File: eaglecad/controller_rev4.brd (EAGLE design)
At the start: 70 x 29.5 mm, 85 parts, among them J1 1.27MM-SWD-CONNECTOR, U101 TCAN330, U200 TPS63070, U300 STSPIN230, U301 TSV991ILT, U302 AS5047P, U400 STSPIN250, U401 TSV991ILT, X101 ABM10-16MHz

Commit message: Prelim final rev completed + design overhaul
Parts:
- removed J1: 1.27MM-SWD-CONNECTOR, J-CNC-3220-10-0100-00-ARM-SWD-port:1.27MM_2X5
- removed JP1, JP2: (no value), pinhead:1X02
- removed JP103: (no value), SparkFun-Connectors:6_PIN_SERIAL_TARGET_SIDE_W_SILK
- removed R310, R311, R415, R416: 0.68, oresat-rcl:.0805-B-NOSILK
- removed R312, R313, R417, R418: 2.2k, rcl_custom:.0402-B-NOSILK
- removed R315: 10k, rcl_custom:.0402-B-NOSILK
- added JP101, JP501: (no value), pinhead:1X02
- added JP502: (no value), SparkFun-Connectors:6_PIN_SERIAL_TARGET_SIDE_W_SILK
- added JP503: 1.27MM-SWD-CONNECTOR, J-CNC-3220-10-0100-00-ARM-SWD-port:1.27MM_2X5
- added R303, R307: 2.2k, rcl_custom:.0402-B-NOSILK
- added R304: 680, rcl_custom:.0402-B-NOSILK
- added R305, R306, R411, R412: 0.68, oresat-rcl:.0805-B-NOSILK
- added R403, R404: 330, rcl_custom:.0402-B-NOSILK
- C306: value 680p -> 4.7u; device rcl_custom:.0402-B-NOSILK -> oresat-rcl:.0603-B-NOSILK
- C307, C408: value 680p -> 100n
- C308: value 100n -> 680p
- C309, C410: value 4.7u -> 680p; device oresat-rcl:.0603-B-NOSILK -> rcl_custom:.0402-B-NOSILK
- C406: value 22n -> 2.2n
- C407: value 2.2n -> 22n
- C409: value 100n -> 4.7u; device rcl_custom:.0402-B-NOSILK -> oresat-rcl:.0603-B-NOSILK
- R309: value 680 -> 10k
- R405: value 330 -> 100k
- R406: value 330 -> 18k
- R409: value 100k -> 2.2k
- R410: value 18k -> 680
- R414: value 680 -> 2.2k
- moved R309 44.4 mm to (20.0, 22.5), flipped to the bottom
- moved C306 43.8 mm to (24.0, 23.7), turned to 180 degrees
- moved C307 41.4 mm to (26.1, 24.6)
- moved R406 40.0 mm to (27.4, 9.01), turned to 270 degrees
- moved R405 40.0 mm to (26.4, 9.01)
- moved U301 39.5 mm to (23.8, 26.0)
- moved TP1 38.3 mm to (12.8, 6.45)
- moved C301 38.0 mm to (12.1, 20.3), flipped to the bottom, turned to 180 degrees
- moved R308 37.1 mm to (25.1, 28.1), turned to 0 degrees
- moved C309 37.0 mm to (26.7, 26.5), turned to 90 degrees
- moved C302 36.7 mm to (12.1, 21.8), flipped to the bottom, turned to 180 degrees
- moved JP102 36.2 mm to (16.4, 2.00)
- moved C308 36.1 mm to (23.1, 28.1), turned to 0 degrees
- moved C303 35.5 mm to (12.1, 23.3), flipped to the bottom, turned to 180 degrees
- moved C401 31.5 mm to (18.1, 8.57), flipped to the bottom
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- renumbered U$1 to U100
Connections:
- removed net UART_XT: U100.12
- new net UART_TX: U$2.6, U100.12
- net 250_REF: now also C406.1, R405.2, R406.1; no longer C407.1, R409.2, R410.1
- net 3.3V: now also C306.1, C307.1, C408.1, JP503.VTREF, R303.2, R309.1, R405.1, R409.2; no longer C308.1, C309.1, C410.1, J1.VTREF, R308.2, R315.1, R409.1, R413.2
- net AS5047_MOSI: now also R309.2; no longer R315.2
- net BLDC_CURR_FDB: now also C309.1, R307.2; no longer C307.1, R313.2
- net GND: now also C307.2, JP101.2, JP502.P$6, JP503.GND, JP503.GND@2, R305.1, R306.1, R308.1, R406.2, R411.2, R412.2, R414.1; no longer C309.2, J1.GND, J1.GND@2, JP1.2, JP103.P$6, R310.1, R311.1, R312.1, R410.2, R415.2, R416.2, R417.1
- net MAG_CURR_FDB: now also R413.2; no longer R418.2
- net MAG_DIR: now also R403.2; no longer R405.2
- net MAG_PWM: now also R404.2; no longer R406.2
- net N$11: now also R413.1, R414.2; no longer R417.2, R418.1
- net N$12: now also C309.2, R307.1, R308.2; no longer C307.2, R312.2, R313.1
- net N$2: now also C407.1; no longer C406.1
- net N$3: now also R404.1; no longer R406.1
- net N$5: now also R403.1; no longer R405.1
- net N$7: now also C410.1, R409.1, R410.2; no longer C408.1, R413.1, R414.2
- net N$9: now also C308.1, R303.1, R304.2; no longer C306.1, R308.1, R309.2
- net NRESET_D: now also JP503.!RESET, U$3.7; no longer J1.!RESET
- net NRST: now also U$2.7
- net QUAD_A: now also U$2.4
- net QUAD_A_D: now also JP501.1, U$3.4; no longer JP2.1
- net QUAD_B: now also U$2.3
- net QUAD_B_D: now also JP501.2, U$3.3; no longer JP2.2
- net SENSE_BLDC: now also R304.1, R305.2, R306.2; no longer R309.1, R310.2, R311.2
- net SENSE_MAG: now also R410.1, R411.1, R412.1; no longer R414.1, R415.1, R416.1
- net SWCLK: now also U$2.9
- net SWCLK_D: now also JP503.SWDCLK, U$3.9; no longer J1.SWDCLK
- net SWDIO: now also U$2.8
- net SWDIO_D: now also JP503.SWDIO, U$3.8; no longer J1.SWDIO
- net UART_RX: now also U$2.5
- net USART_RX_D: now also JP502.P$3, U$3.5; no longer JP103.P$3
- net USART_TX_D: now also JP502.P$2, U$3.6; no longer JP103.P$2
- net VBUS: now also JP101.1, JP502.P$4; no longer JP1.1, JP103.P$4
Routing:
- net GND: track 14.8 -> 40.5 mm, vias 22 -> 102
- net CAN_SILENT: track 0.00 -> 22.4 mm
- net MAG_CURR_FDB: track 1.00 -> 22.9 mm, vias 0 -> 3
- net BLDC_CURR_FDB: track 0.00 -> 21.4 mm, vias 0 -> 2
- net SENSE_BLDC: track 0.00 -> 21.1 mm, vias 0 -> 3
- net QUAD_A: track 0.00 -> 20.2 mm, vias 0 -> 1
- net SWCLK: track 0.00 -> 20.1 mm, vias 0 -> 2
- net SWDIO: track 0.00 -> 20.0 mm, vias 0 -> 2
- net QUAD_B: track 0.00 -> 19.5 mm, vias 0 -> 1
- net 3.3V: track 8.73 -> 27.6 mm, vias 2 -> 16
- net CAN_RX: track 0.00 -> 17.5 mm
- net SENSE_MAG: track 0.00 -> 17.5 mm, vias 0 -> 5
- net CAN_TX: track 0.00 -> 16.0 mm
- net BLDC_STBY: track 0.00 -> 15.9 mm, vias 0 -> 2
- net BLDC_INUH: track 0.00 -> 14.5 mm
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- added copper zone on layer 15, net 3.3V
- added copper zone on layer 1, net GND
- added copper zone on layer 16, net GND
- added copper zone on layer 2, net GND
- added copper zone on layer 15, net VBUS
- added copper zone on layer 16, net VBUS
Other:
- board size 70 x 29.5 mm -> 57 x 29.5 mm

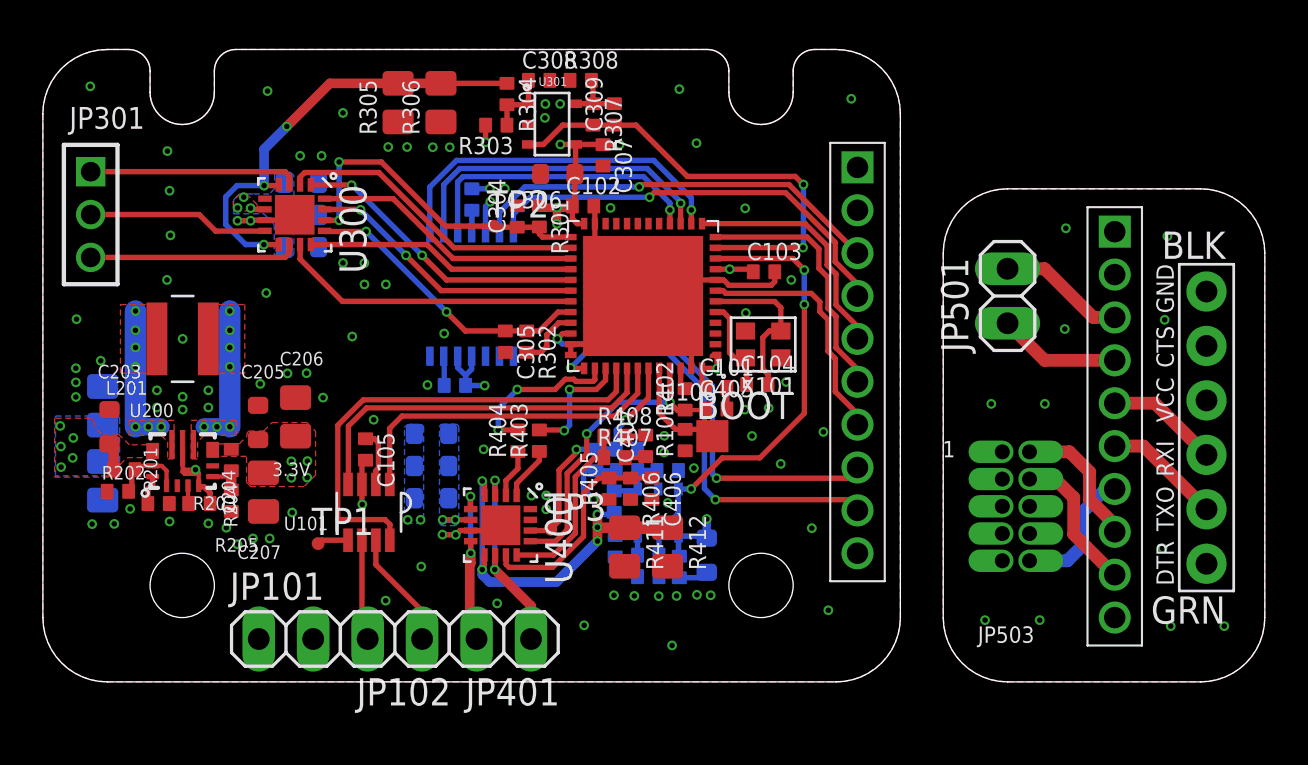
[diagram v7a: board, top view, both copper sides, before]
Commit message: Programing addapter board
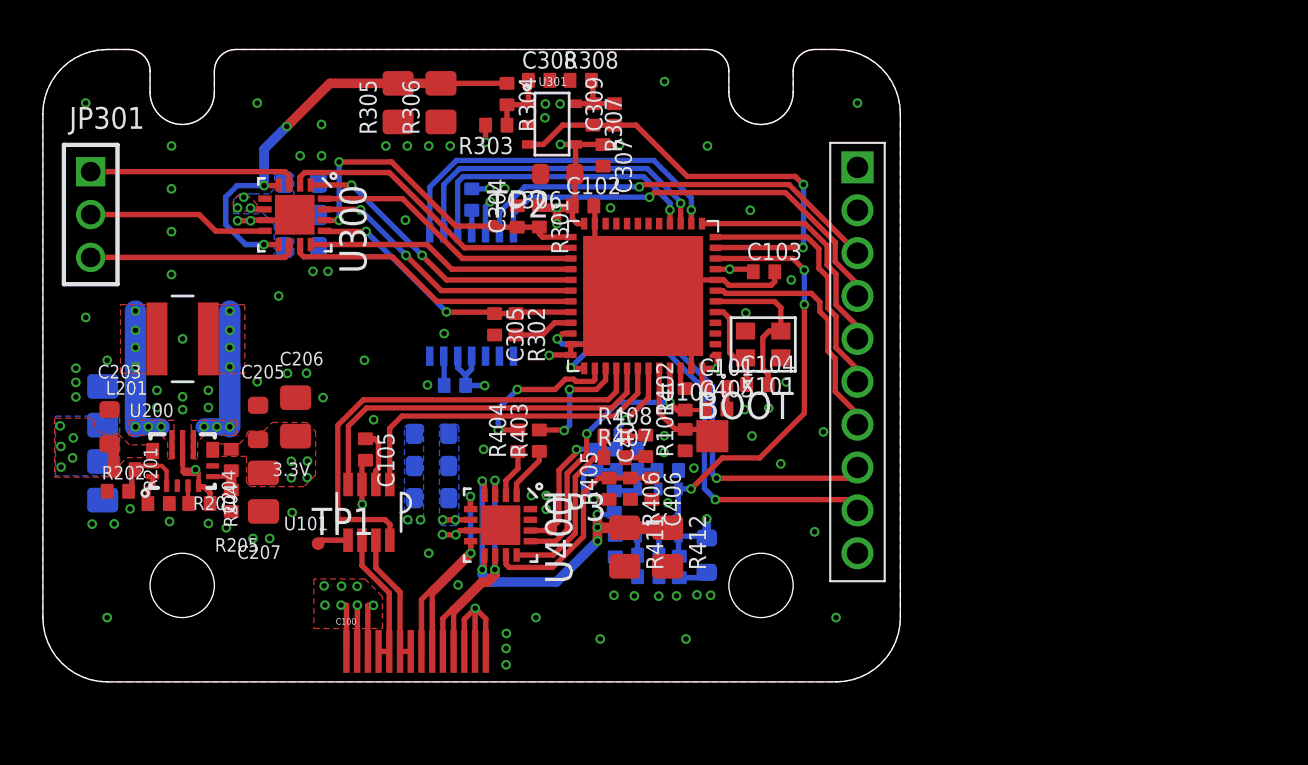
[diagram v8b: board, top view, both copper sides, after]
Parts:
- removed JP101, JP102, JP401, JP501: (no value), pinhead:1X02
- removed JP502: (no value), SparkFun-Connectors:6_PIN_SERIAL_TARGET_SIDE_W_SILK
- removed JP503: 1.27MM-SWD-CONNECTOR, J-CNC-3220-10-0100-00-ARM-SWD-port:1.27MM_2X5
- removed U$3: DEBUG_CON, oresat-ACS_driver_board:DEBUG_CON
- added C100: CARD CONN, oresat-ACS_driver_board:LOW-PROFILE_CONNECTOR(TAB)
- moved C305 0.95 mm to (21.1, 16.7)
- moved R302 0.95 mm to (22.1, 16.7)
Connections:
- net N$1 renamed CLK2
- net N$11 renamed M_IN-
- net N$12 renamed B_IN-
- net N$2 renamed TOFF1
- net N$3 renamed M_PWM
- net N$4 renamed CLK1
- net N$5 renamed M_PH
- net N$7 renamed M_IN+
- net N$9 renamed B_IN+
- removed net NRESET_D: JP503.!RESET, U$3.7
- removed net QUAD_A_D: JP501.1, U$3.4
- removed net QUAD_B_D: JP501.2, U$3.3
- removed net SWCLK_D: JP503.SWDCLK, U$3.9
- removed net SWDIO_D: JP503.SWDIO, U$3.8
- removed net USART_RX_D: JP502.P$3, U$3.5
- removed net USART_TX_D: JP502.P$2, U$3.6
- net 3.3V: no longer JP503.VTREF, U$3.2
- net CAN_H: now also C100.6, C100.7; no longer JP102.1
- net CAN_L: now also C100.4, C100.5; no longer JP102.2
- net GND: now also C100.12, C100.13, C100.14; no longer JP101.2, JP502.P$6, JP503.GND, JP503.GND@2, U$3.10
- net OUT1: now also C100.10, C100.11; no longer JP401.1
- net OUT2: now also C100.8, C100.9; no longer JP401.2
- net VBUS: now also C100.1, C100.2, C100.3; no longer JP101.1, JP502.P$4, U$3.1
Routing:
- net GND: track 40.5 -> 47.9 mm, vias 102 -> 98
- net VBUS: track 3.87 -> 10.9 mm, vias 10 -> 17
- net SWCLK_D: track 6.82 -> 0.00 mm
- net SWDIO_D: track 6.47 -> 0.00 mm
- net NRESET_D: track 6.28 -> 0.00 mm
- net QUAD_B_D: track 5.94 -> 0.00 mm
- net QUAD_A_D: track 5.72 -> 0.00 mm
- net USART_TX_D: track 5.50 -> 0.00 mm
- net USART_RX_D: track 5.28 -> 0.00 mm
- net OUT2: track 7.95 -> 12.4 mm
- net OUT1: track 9.53 -> 12.7 mm
- net CAN_L: track 4.72 -> 6.22 mm
- net BLDC_FAULT: track 13.8 -> 13.1 mm
- net CAN_H: track 5.51 -> 6.16 mm
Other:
- board size 57 x 29.5 mm -> 40 x 29.5 mm
